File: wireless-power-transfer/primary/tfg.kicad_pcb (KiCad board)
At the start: 2 copper layers, 160 x 100 mm, 31 parts, among them J1 CONN_01X06, J2 Screw_Terminal_1x02, J3 BARREL_JACK, Q1 IRLB8721PBF, Q2 IRLB8721PBF, Q3 IRLB8721PBF, Q4 IRLB8721PBF, U1 PIC18F45K20-I/PT, U2 IR2110, U3 IR2110, U4 R-78E15, U5 R-78E3.3, U6 XBEE_Wi-Fi

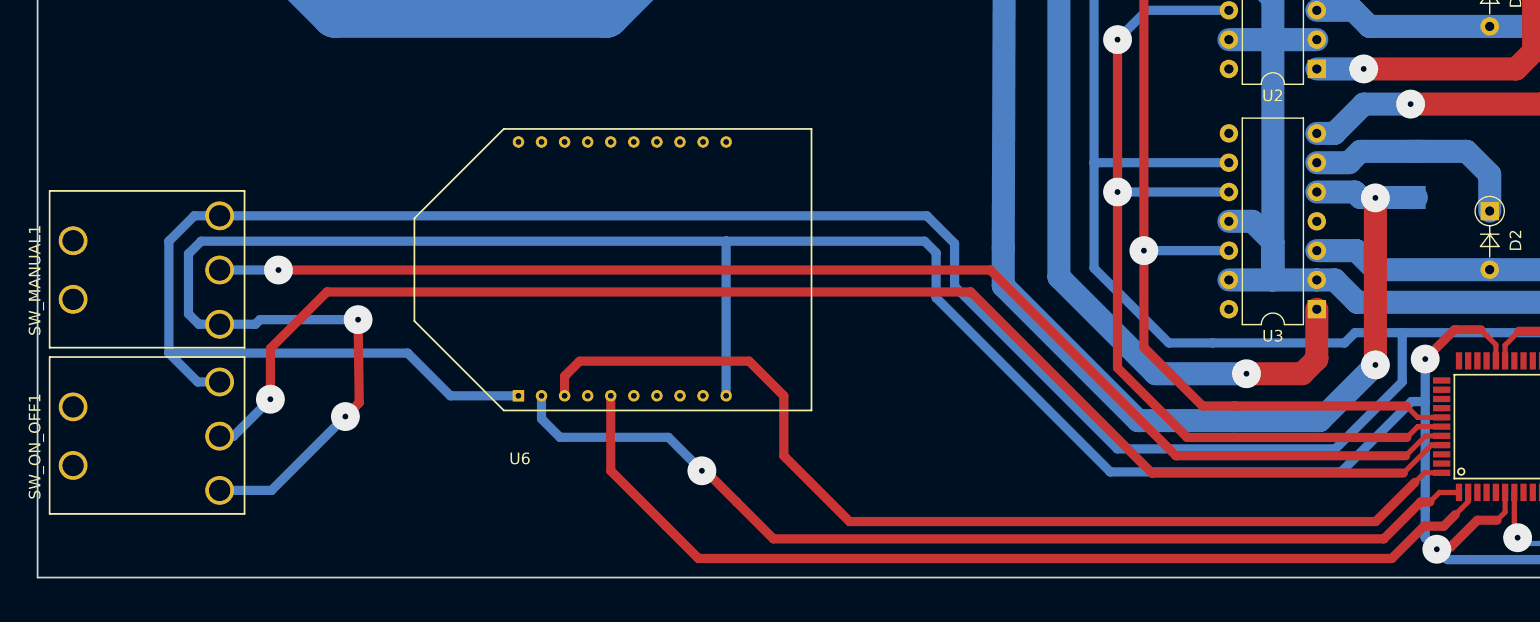
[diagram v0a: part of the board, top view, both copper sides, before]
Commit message: New version with changed interruptors, improved routing layout, fixed 3d designs and Wi-Fi module, among other minor changes.
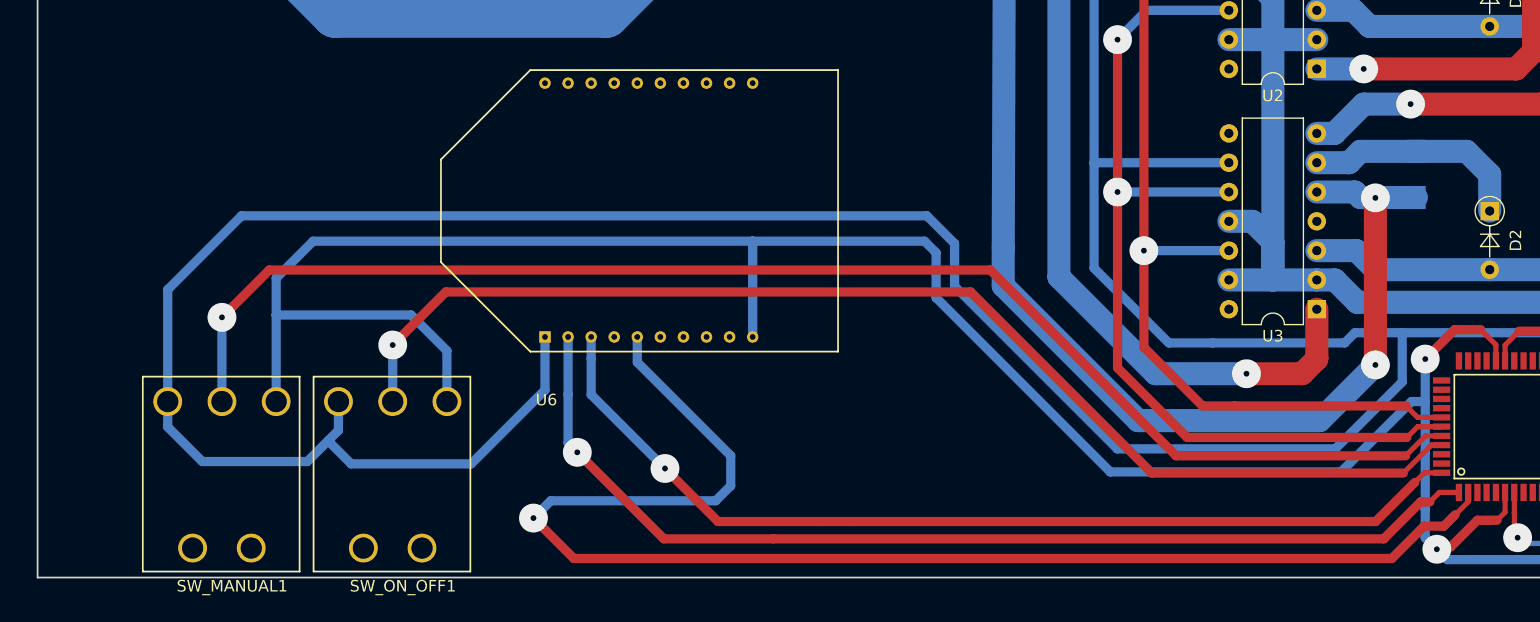
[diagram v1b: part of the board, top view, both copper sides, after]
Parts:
- moved SW_MANUAL1 16.7 mm to (97.0, 131.7), turned to 0 degrees
- moved SW_ON_OFF1 10.4 mm to (111.8, 131.7), turned to 0 degrees
- moved U6 5.59 mm to (129.7, 126.1)
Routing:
- net Net-(U1-Pad2): track 86.8 -> 119.8 mm, vias 0 -> 1
- net Net-(C1-Pad2): track 567.8 -> 544.5 mm, vias 4 -> 2
- net Net-(SW_ON_OFF1-Pad2): track 121.2 -> 105.2 mm
- net /+3.3V: track 341.7 -> 355.0 mm
- net Net-(SW_MANUAL1-Pad2): track 113.3 -> 122.1 mm
- net Net-(U1-Pad1): track 87.5 -> 91.5 mm
- net Net-(U1-Pad44): track 88.8 -> 85.0 mm, vias 0 -> 1

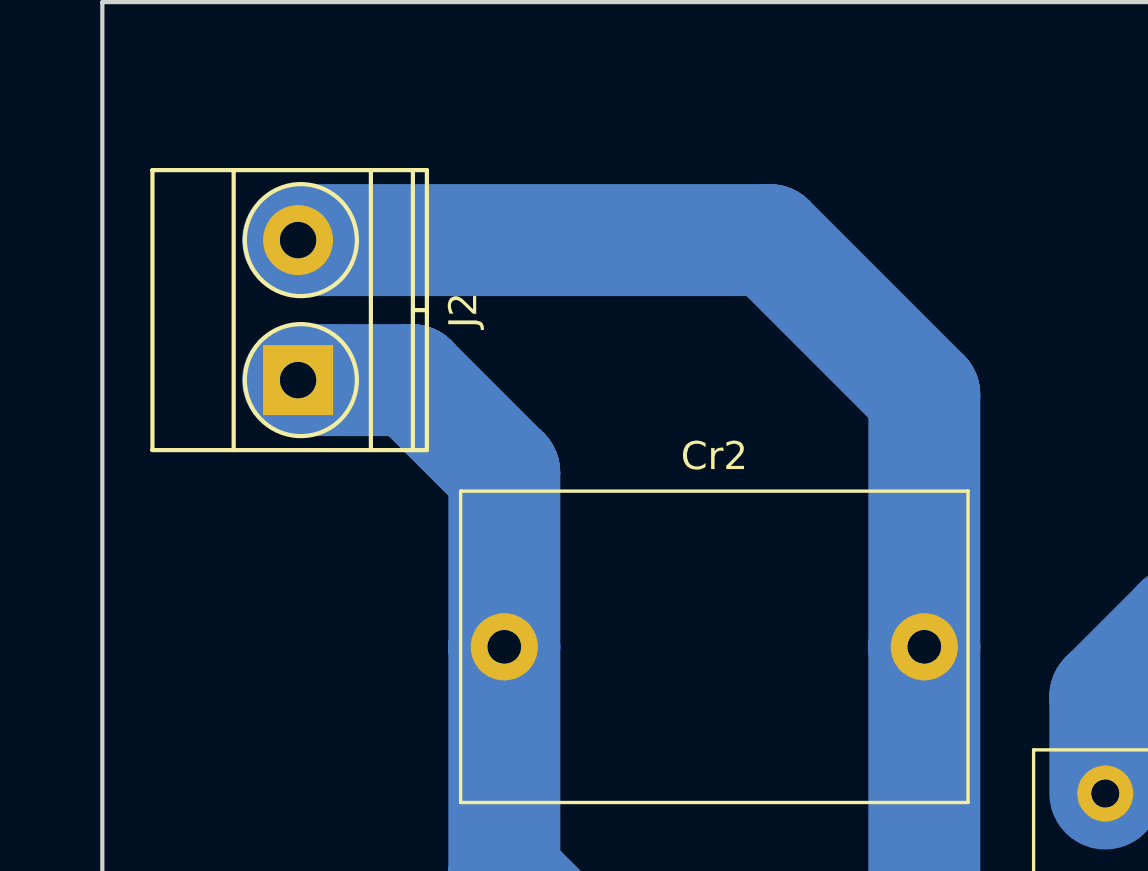
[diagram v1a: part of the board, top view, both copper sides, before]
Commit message: Orientation of the primary coil connector fixed.
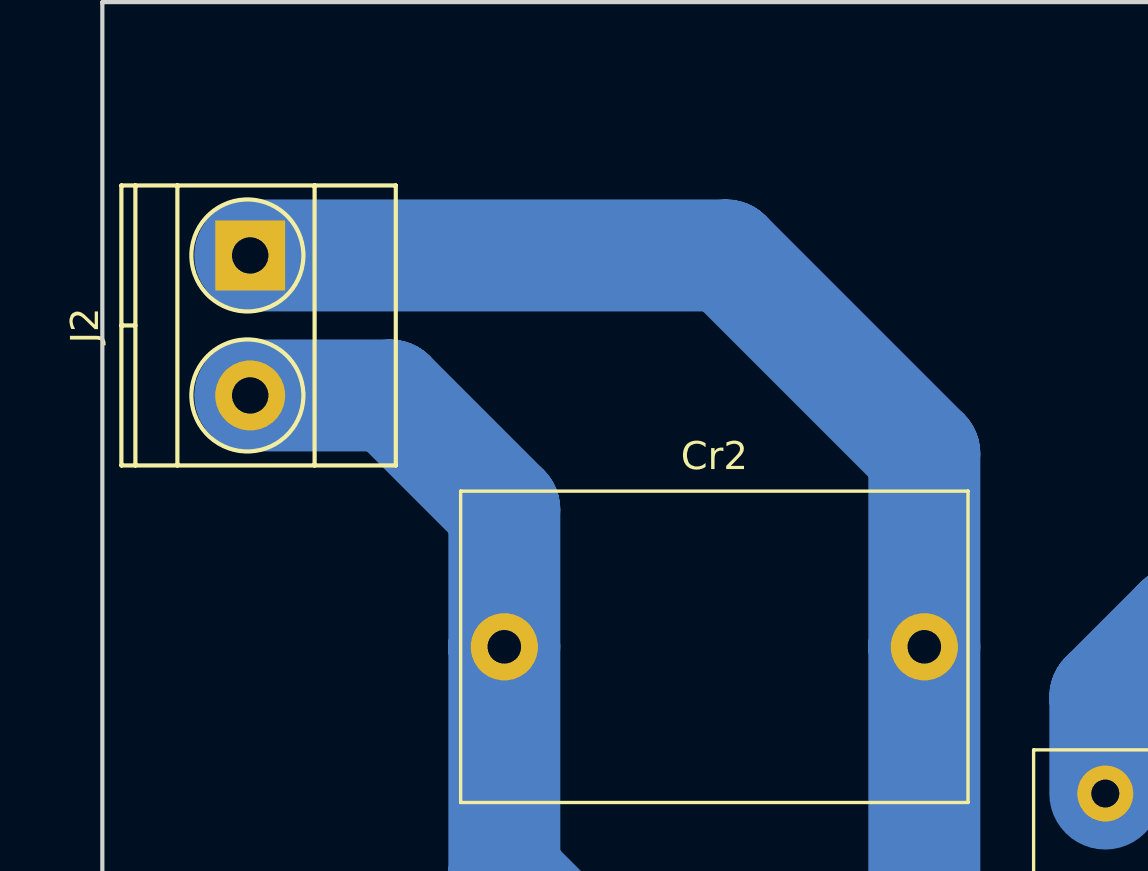
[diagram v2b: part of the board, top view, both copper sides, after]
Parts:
- moved J2 4.77 mm to (91.0, 56.0), turned to 270 degrees
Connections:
- J2 pad 1: Net-(Cboot2-Pad2) -> Net-(Cf1-Pad1)
- J2 pad 2: Net-(Cf1-Pad1) -> Net-(Cboot2-Pad2)
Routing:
- net Net-(Cboot2-Pad2): track 259.6 -> 260.3 mm
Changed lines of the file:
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@@
   )
   (setup
-    (last_trace_width 0.8)
+    (last_trace_width 4)
     (user_trace_width 0.45)
     (user_trace_width 0.8)
@@
   )
   (module Connectors_Terminal_Blocks:TerminalBlock_Pheonix_MKDS1.5-2pol (layer F.Cu)
-    (at 92.71 60.452 90)
+    (at 91 56 270)
     (descr "2-way 5mm pitch terminal block, Phoenix MKDS series")
-    (fp_text reference J2 (at 2.5 5.9 90) (layer F.SilkS)
-      (effects (font (size 1 1) (thickness 0.15)))
-    )
-    (fp_text value Screw_Terminal_1x02 (at 2.5 -6.6 90) (layer F.Fab)
+    (fp_text reference J2 (at 2.5 5.9 270) (layer F.SilkS)
+      (effects (font (size 1 1) (thickness 0.15)))
+    )
+    (fp_text value Screw_Terminal_1x02 (at 2.5 -6.6 270) (layer F.Fab)
       (effects (font (size 1 1) (thickness 0.15)))
     )
@@
     (fp_line (start 7.5 -5.2) (end -2.5 -5.2) (layer F.SilkS) (width 0.15))
     (fp_line (start -2.5 -5.2) (end -2.5 4.6) (layer F.SilkS) (width 0.15))
-    (pad 1 thru_hole rect (at 0 0 90) (size 2.5 2.5) (drill 1.3) (layers *.Cu *.Mask)
+    (pad 1 thru_hole rect (at 0 0 270) (size 2.5 2.5) (drill 1.3) (layers *.Cu *.Mask)
+      (net 10 "Net-(Cf1-Pad1)"))
+    (pad 2 thru_hole circle (at 5 0 270) (size 2.5 2.5) (drill 1.3) (layers *.Cu *.Mask)
       (net 9 "Net-(Cboot2-Pad2)"))
-    (pad 2 thru_hole circle (at 5 0 90) (size 2.5 2.5) (drill 1.3) (layers *.Cu *.Mask)
-      (net 10 "Net-(Cf1-Pad1)"))
     (model Terminal_Blocks.3dshapes/TerminalBlock_Pheonix_MKDS1.5-2pol.wrl
       (at (xyz 0.0984 0 0))
@@
   (segment (start 209.582 110.014) (end 205.232 110.014) (width 2) (layer B.Cu) (net 8))
   (segment (start 211.582 112.014) (end 209.582 110.014) (width 2) (layer B.Cu) (net 8))
+  (segment (start 100.076 69.977) (end 100.076 65.076) (width 4) (layer B.Cu) (net 9) (status 400000))
+  (segment (start 96 61) (end 91 61) (width 4) (layer B.Cu) (net 9) (status 800000))
+  (segment (start 100.076 65.076) (end 96 61) (width 4) (layer B.Cu) (net 9))
   (segment (start 174.244 55.88) (end 169.82 55.88) (width 2) (layer B.Cu) (net 9))
   (segment (start 160.1 65.8) (end 160.1 75.946) (width 4) (layer B.Cu) (net 9))
@@
   (segment (start 174.244 75.692) (end 169.545 75.692) (width 2) (layer B.Cu) (net 9))
   (segment (start 169.545 75.692) (end 163.957 75.692) (width 2) (layer B.Cu) (net 9))
-  (segment (start 100.076 69.977) (end 100.076 63.754) (width 4) (layer B.Cu) (net 9))
-  (segment (start 100.076 63.754) (end 96.774 60.452) (width 4) (layer B.Cu) (net 9))
-  (segment (start 96.774 60.452) (end 92.71 60.452) (width 4) (layer B.Cu) (net 9))
+  (segment (start 91 56) (end 108 56) (width 4) (layer B.Cu) (net 10) (status 400000))
+  (segment (start 115.076 63.076) (end 115.076 69.977) (width 4) (layer B.Cu) (net 10) (status 800000))
+  (segment (start 108 56) (end 115.076 63.076) (width 4) (layer B.Cu) (net 10))
   (segment (start 115.076 79.107) (end 115.076 84.924) (width 4) (layer B.Cu) (net 10))
   (segment (start 115.076 69.977) (end 115.076 79.107) (width 4) (layer B.Cu) (net 10))
@@
   (segment (start 120.756 86) (end 121.539 85.217) (width 4) (layer B.Cu) (net 10))
   (segment (start 114 86) (end 120.756 86) (width 4) (layer B.Cu) (net 10))
-  (segment (start 115.076 69.977) (end 115.076 60.974) (width 4) (layer B.Cu) (net 10))
-  (segment (start 115.076 60.974) (end 109.554 55.452) (width 4) (layer B.Cu) (net 10))
-  (segment (start 109.554 55.452) (end 92.71 55.452) (width 4) (layer B.Cu) (net 10))
   (segment (start 121.539 85.217) (end 121.539 87.249) (width 4) (layer B.Cu) (net 10))
   (segment (start 121.539 87.249) (end 125.095 90.805) (width 4) (layer B.Cu) (net 10))

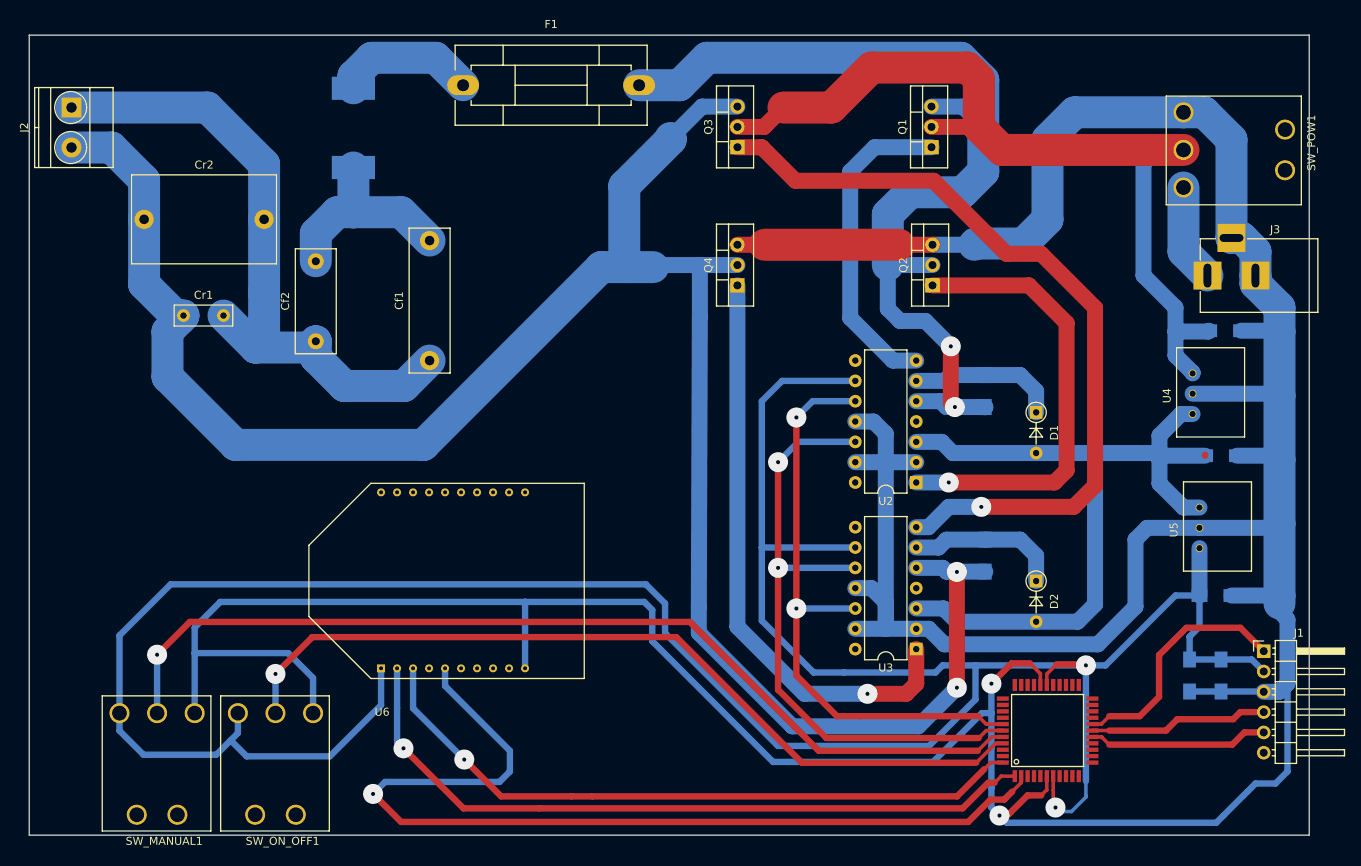
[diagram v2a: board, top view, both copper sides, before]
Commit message: LEDs for power and charging indication added.
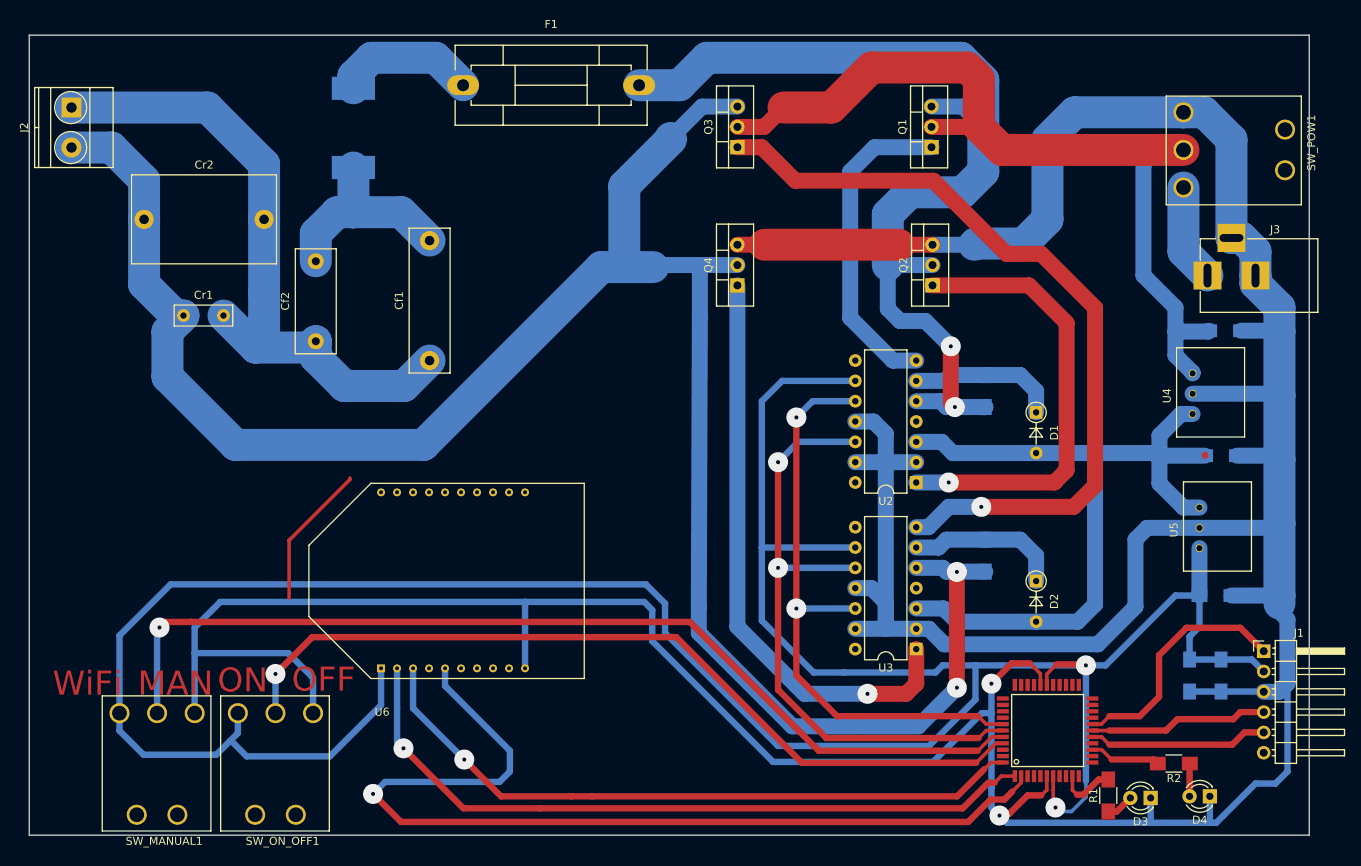
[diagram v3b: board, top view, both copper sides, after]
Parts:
- added D3: LED, LEDs:LED_D3.0mm, F.Cu at (225.9, 142.3)
- added D4: LED, LEDs:LED_D3.0mm, F.Cu at (233.3, 142.1)
- added R1: R, Resistors_SMD:R_1206_HandSoldering, F.Cu at (220.6, 142.0)
- added R2: R, Resistors_SMD:R_1206_HandSoldering, F.Cu at (228.8, 138.0)
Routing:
- net (no net): track 0.09 -> 18.2 mm
- net Net-(R2-Pad2): track 0.00 -> 8.90 mm
- net Net-(R1-Pad2): track 0.00 -> 7.26 mm
- net Net-(C1-Pad2): track 544.5 -> 551.5 mm
- net Net-(D4-Pad2): track 0.00 -> 4.12 mm
- net Net-(D3-Pad2): track 0.00 -> 3.46 mm
- net Net-(SW_MANUAL1-Pad2): track 122.1 -> 124.5 mm
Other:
- board text added: "MAN"
- board text added: "OFF"
- board text added: "ON"
- board text added: "WiFi"

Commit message: fixed MOSFET sizes and some excessively small pads.
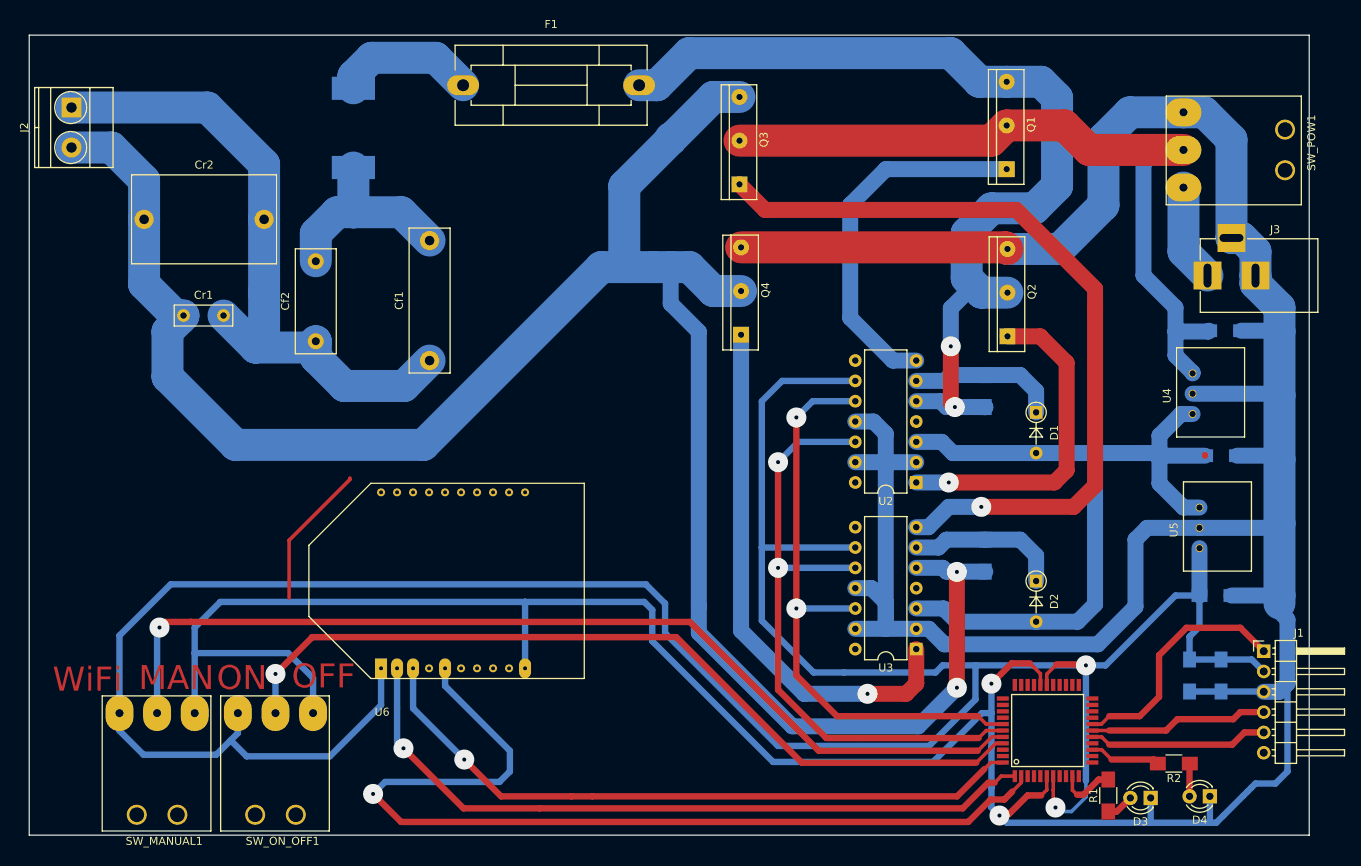
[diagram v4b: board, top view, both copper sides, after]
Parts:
- Q1, Q2, Q3, Q4: footprint TO_SOT_Packages_THT:TO-220-3_Vertical -> componentesGIT:TO-247AC
- U1: footprint componentes:PIC18F45K20 -> componentesGIT:PIC18F45K20
- moved Q2 11.3 mm to (208.0, 84.6)
- moved Q1 9.79 mm to (207.9, 63.7)
- moved Q4 6.18 mm to (174.7, 84.4)
- moved Q3 4.65 mm to (174.5, 65.6)
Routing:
- net Net-(C5-Pad1): track 111.3 -> 96.3 mm
- net Net-(Q2-Pad1): track 56.6 -> 41.6 mm
- net Net-(Q4-Pad1): track 73.3 -> 67.0 mm
- net Net-(Q1-Pad1): track 40.2 -> 46.0 mm
- net Net-(Cboot2-Pad2): track 260.3 -> 264.3 mm
- net Net-(Cboot1-Pad2): track 123.6 -> 122.2 mm
- net Net-(C1-Pad2): track 551.5 -> 550.2 mm
- net Net-(Q3-Pad1): track 99.7 -> 99.2 mm
